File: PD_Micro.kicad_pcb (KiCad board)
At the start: 2 copper layers, 40 parts, among them J1 Conn_01x02, J2 Conn_01x02, J3 Conn_01x02, Q1 DMP3017SFK, Q2 DTC143E, U1 TPS62175DQC, U2 SRV05-4, U3 Pico, U4 FUSB302BMPX, U5 ACS723xMATR-10AB, U6 oledSym

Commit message: no drc errors
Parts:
- added SW1: SW_DPST_x2, Button_Switch_SMD:SW_SPDT_PCM12, F.Cu at (210.7, 135.1)
- added SW2: SW_Push, Button_Switch_SMD:SW_SPST_TL3305C, F.Cu at (230.9, 134.4)
- added SW4: SW_DPST_x2, Button_Switch_SMD:SW_SPDT_PCM12, F.Cu at (220.4, 135.1)
- added SW5: SW_DIP_x06, Button_Switch_THT:SW_DIP_SPSTx06_Slide_9.78x17.42mm_W7.62mm_P2.54mm, F.Cu at (208.9, 127.6)
- added SW6: SW_Push, Button_Switch_SMD:SW_SPST_TL3305C, F.Cu at (231.0, 126.4)
- moved D2 68.4 mm to (215.0, 115.2)
- moved J1 62.4 mm to (232.4, 108.5)
- moved J3 59.8 mm to (232.0, 101.0), turned to -90 degrees
- moved J2 55.0 mm to (235.3, 95.7), turned to 180 degrees
- moved U6 54.3 mm to (191.5, 124.3), turned to 0 degrees
- moved H3 46.9 mm to (176.7, 88.6)
- moved H4 46.0 mm to (176.7, 114.0)
- moved R9 45.0 mm to (173.5, 105.8), turned to 0 degrees
- moved C12 43.1 mm to (172.8, 107.9), turned to 0 degrees
- moved U1 42.1 mm to (189.0, 97.3)
- moved C13 41.8 mm to (180.6, 95.8)
- moved C6 41.8 mm to (178.6, 95.8)
- moved C7 41.8 mm to (176.5, 95.8)
- moved C8 41.8 mm to (174.5, 95.8)
- moved R1 41.8 mm to (183.3, 95.8)
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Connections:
- net D10 renamed ENOUT
- R11 pad 2: D2 -> SDA
- R12 pad 2: D3 -> SCL
- U3 pad 10: Net-(U3-Pad10) -> SCL
- U3 pad 11: unconnected-(U3-Pad11) -> EN5V
- U3 pad 12: unconnected-(U3-Pad12) -> EN9V
- U3 pad 14: unconnected-(U3-Pad14) -> EN12V
- U3 pad 15: unconnected-(U3-Pad15) -> EN15V
- U3 pad 16: unconnected-(U3-Pad16) -> EN20V
- U3 pad 17: unconnected-(U3-Pad17) -> ENPSU
- U3 pad 19: unconnected-(U3-Pad19) -> Net-(SW4-Pad2)
- U3 pad 20: unconnected-(U3-Pad20) -> Net-(U3-Pad20)
- U3 pad 4: unconnected-(U3-Pad4) -> Net-(U3-Pad4)
- U3 pad 5: unconnected-(U3-Pad5) -> Net-(U3-Pad5)
- U3 pad 6: unconnected-(U3-Pad6) -> Net-(SW1-Pad2)
- U3 pad 7: unconnected-(U3-Pad7) -> INT_N
- U3 pad 9: Net-(U3-Pad9) -> SDA
- U4 pad 5: D7 -> INT_N
- U4 pad 6: D3 -> SCL
- U4 pad 7: D2 -> SDA
- U6 pad 3: Net-(U3-Pad10) -> SCL
- U6 pad 4: Net-(U3-Pad9) -> SDA
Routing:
- net Net-(U3-Pad5): track 0.00 -> 68.6 mm, vias 0 -> 1
- net Net-(U3-Pad4): track 0.00 -> 60.9 mm, vias 0 -> 1
- net Net-(D2-Pad4): track 0.00 -> 41.5 mm
- net Net-(SW1-Pad2): track 0.00 -> 40.8 mm, vias 0 -> 3
- net SCL: track 0.00 -> 39.2 mm, vias 0 -> 3
- net SDA: track 0.00 -> 27.5 mm, vias 0 -> 2
- net Net-(SW4-Pad2): track 0.00 -> 24.5 mm, vias 0 -> 1
- net GND: track 2.59 -> 27.1 mm
- net INT_N: track 0.00 -> 14.6 mm, vias 0 -> 1
- net EN9V: track 0.00 -> 12.5 mm
- net EN5V: track 0.00 -> 12.5 mm
- net EN20V: track 0.00 -> 11.4 mm
- net EN15V: track 0.00 -> 11.4 mm
- net EN12V: track 0.00 -> 11.4 mm
- net ENPSU: track 0.00 -> 11.4 mm
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- added copper zone on B.Cu, net /OUT
- added copper zone on F.Cu, net /OUT
- removed copper zone on B.Cu, net GND
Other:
- board outline added: 72.6 x 53.7 mm
- board text added: "12V"
- board text added: "15V"
- board text added: "20V"
- board text added: "5V"
- board text added: "9V"
- board text added: "DOWN"
- board text added: "Max A"
- board text added: "OFF"
- board text added: "ON"
- board text added: "PSU Mode"
- board text added: "UP"
- board text added: "V"

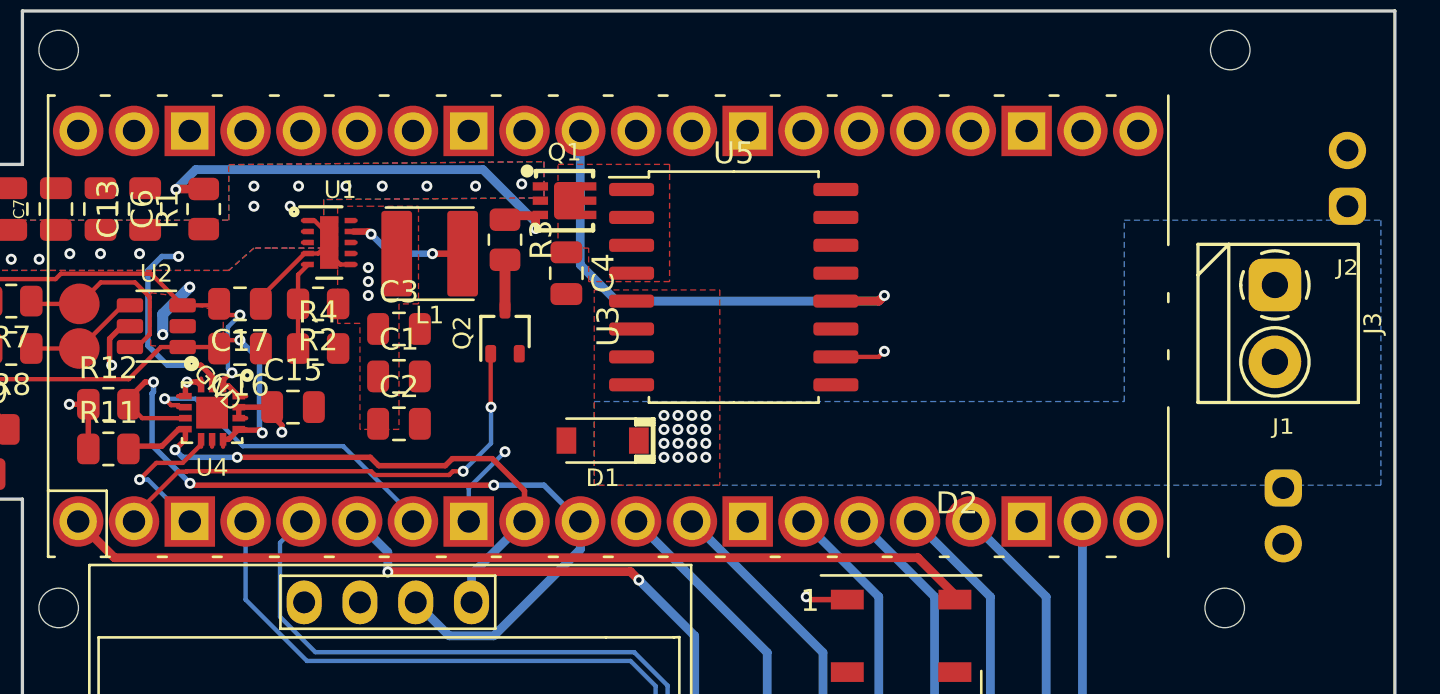
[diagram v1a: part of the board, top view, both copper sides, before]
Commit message: no drcs plus input devices
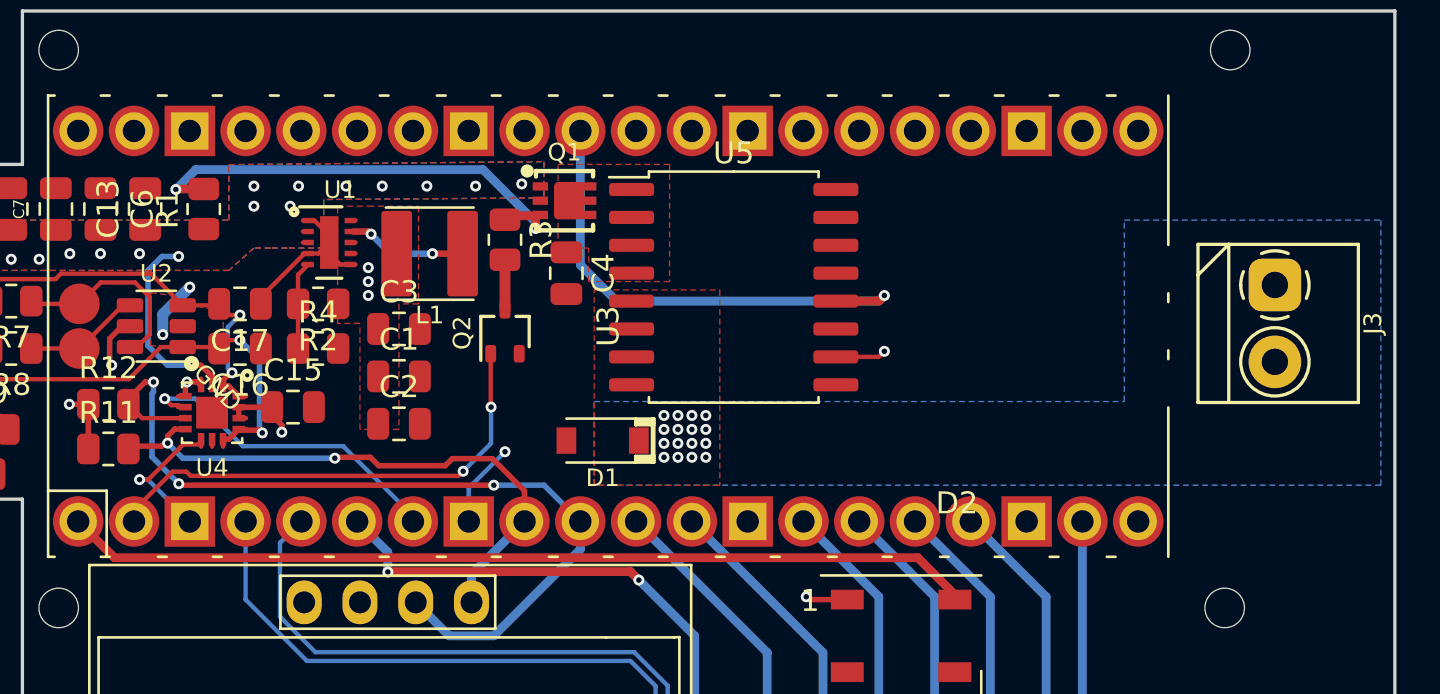
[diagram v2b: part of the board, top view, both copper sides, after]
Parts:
- removed J1, J2: Conn_01x02, -Connector:PinHeader_1x02_P2.54mm_Vertical

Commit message: differential-pair
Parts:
- USB1: moved to B.Cu
- moved C12 10.9 mm to (183.6, 107.1)
- moved USB1 10.3 mm to (173.9, 101.3), turned to 90 degrees
- moved C3 10.2 mm to (202.4, 101.3)
- moved R9 10.2 mm to (183.6, 104.8)
- moved C1 10.2 mm to (202.3, 103.4)
- moved C13 10.2 mm to (190.8, 95.8)
- moved C15 10.2 mm to (197.5, 104.8)
- moved C2 10.2 mm to (202.3, 105.6)
- moved C4 10.2 mm to (210.0, 98.7)
- moved C6 10.2 mm to (188.7, 95.8)
- moved C7 10.2 mm to (186.7, 95.8)
- moved C8 10.2 mm to (184.7, 95.8)
- moved D1 10.2 mm to (211.6, 106.3)
- moved L1 10.2 mm to (203.7, 97.8)
- moved Q1 10.2 mm to (209.9, 95.4)
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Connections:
- net /DN renamed /D_N
- net /DP renamed /D_P
- net Net-(R7-Pad1) renamed /D1_N
- net Net-(R8-Pad1) renamed /D1_P
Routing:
- net ENOUT: track 22.3 -> 0.51 mm, vias 2 -> 0
- net SCL: track 39.5 -> 20.2 mm, vias 3 -> 1
- net SDA: track 27.0 -> 8.78 mm, vias 2 -> 1
- net ADC0: track 23.0 -> 40.8 mm
- net VBUS: track 16.5 -> 0.00 mm, vias 17 -> 15
- net Net-(SW1-Pad2): track 40.8 -> 26.3 mm, vias 3 -> 1
- net /D1_P: track 5.41 -> 19.0 mm
- net GND: track 27.1 -> 15.1 mm, vias 4 -> 2
- net INT_N: track 14.6 -> 5.32 mm
- net /D1_N: track 9.01 -> 18.2 mm
- net /CC1: track 19.1 -> 12.7 mm, vias 2 -> 3
- net /CC2: track 21.6 -> 15.2 mm
- net +5V: track 13.9 -> 11.5 mm, vias 9 -> 8
- net /D_N: track 5.95 -> 3.90 mm, vias 0 -> 1
- net /D_P: track 3.54 -> 3.84 mm, vias 0 -> 1

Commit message: differential-pairs
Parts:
- moved U4 12.8 mm to (206.7, 105.5)
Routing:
- net /CC2: track 15.2 -> 8.54 mm, vias 2 -> 1
- net SCL: track 20.2 -> 13.6 mm, vias 1 -> 0
- net +5V: track 11.5 -> 6.14 mm, vias 8 -> 5
- net INT_N: track 5.32 -> 0.00 mm, vias 1 -> 0
- net /CC1: track 12.7 -> 8.55 mm, vias 3 -> 1
- net SDA: track 8.78 -> 6.95 mm, vias 1 -> 0
- net Net-(D2-Pad4): track 41.3 -> 43.0 mm
- net GND: track 15.1 -> 14.0 mm
- net /D1_N: track 18.2 -> 18.8 mm
- net VBUS: vias 15 -> 14

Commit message: finished pcb
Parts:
- moved H2 24.6 mm to (235.0, 138.0)
- moved H4 24.0 mm to (177.0, 138.0)
- moved U4 13.3 mm to (194.1, 101.3), turned to 0 degrees
- moved R12 10.6 mm to (199.5, 106.7), turned to -90 degrees
- moved R11 7.14 mm to (196.2, 107.2)
- moved H1 5.01 mm to (235.0, 89.0)
- moved C15 1.81 mm to (195.7, 104.6)
- moved SW2 1.42 mm to (230.9, 133.0)
- moved H3 0.54 mm to (177.0, 89.0)
- moved U5 0.13 mm to (217.6, 99.5)
- moved C12 0.13 mm to (183.6, 107.0)
- moved C3 0.05 mm to (202.3, 101.3)
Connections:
- U3 pad 2: ENOUT -> unconnected-(U3-GPIO1-Pad2)
- U3 pad 27: unconnected-(U3-Pad27) -> ENOUT
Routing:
- net Net-(SW1A-B): track 26.3 -> 42.7 mm, vias 1 -> 2
- net SDA: track 6.95 -> 20.9 mm, vias 0 -> 1
- net SCL: track 13.6 -> 27.3 mm, vias 0 -> 1
- net ENOUT: track 0.51 -> 13.9 mm, vias 0 -> 1
- net VBUS: track 0.00 -> 13.0 mm, vias 14 -> 15
- net INT_N: track 0.00 -> 10.2 mm, vias 0 -> 1
- net Net-(U3-GPIO2): track 60.8 -> 69.2 mm
- net /CC1: track 8.55 -> 14.5 mm, vias 1 -> 3
- net /CC2: track 8.54 -> 14.5 mm, vias 1 -> 3
- net +5V: track 6.14 -> 12.1 mm, vias 5 -> 8
- net GND: track 14.0 -> 18.4 mm, vias 2 -> 8
- net Net-(D2-DIN): track 43.0 -> 45.9 mm, vias 0 -> 1
- net Net-(U3-GPIO3): track 68.6 -> 70.2 mm
- net unconnected-(U3-GPIO1-Pad2): track 0.00 -> 0.51 mm
- added copper zone on B.Cu, net GND
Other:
- board size 72.6 x 53.7 mm -> 62 x 53 mm
